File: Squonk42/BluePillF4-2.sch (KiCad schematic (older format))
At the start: 0 parts

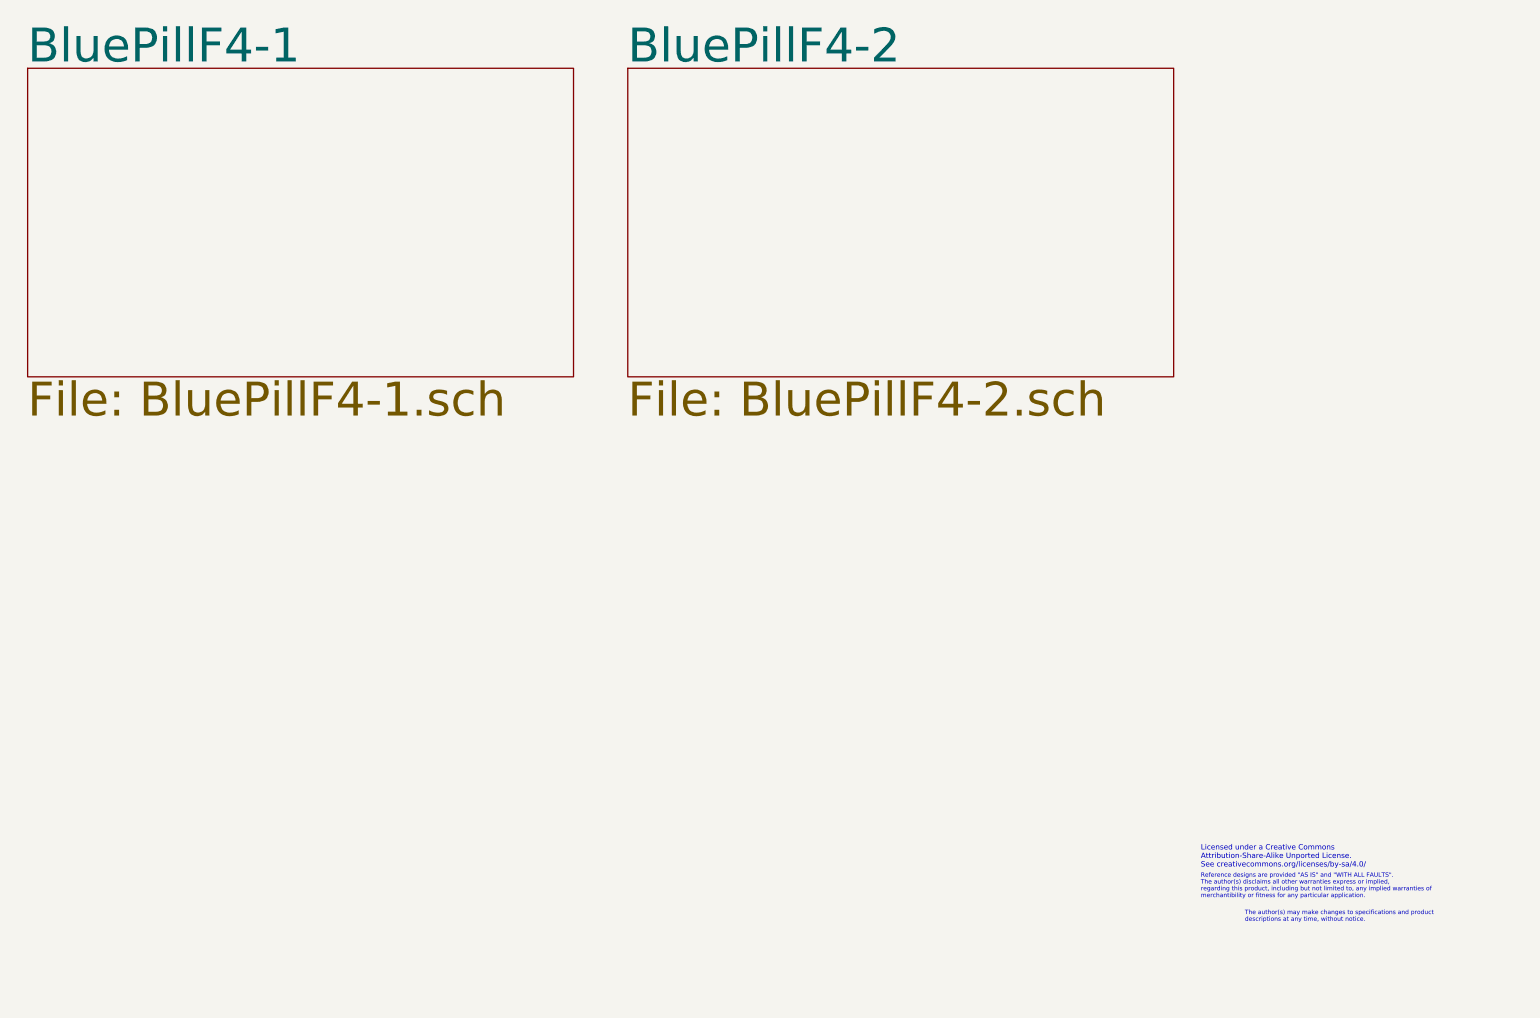
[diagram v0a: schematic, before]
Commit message: Added LiPo battery charger circuit (option) Put AGND on the analog LDO instead of GND Improved the analog power supply filter Aligned the pads for the PC1-PC7 pins with a 1.27 mm pitch. Now PC0 is used for VBUS_EN instead of PC4 previously
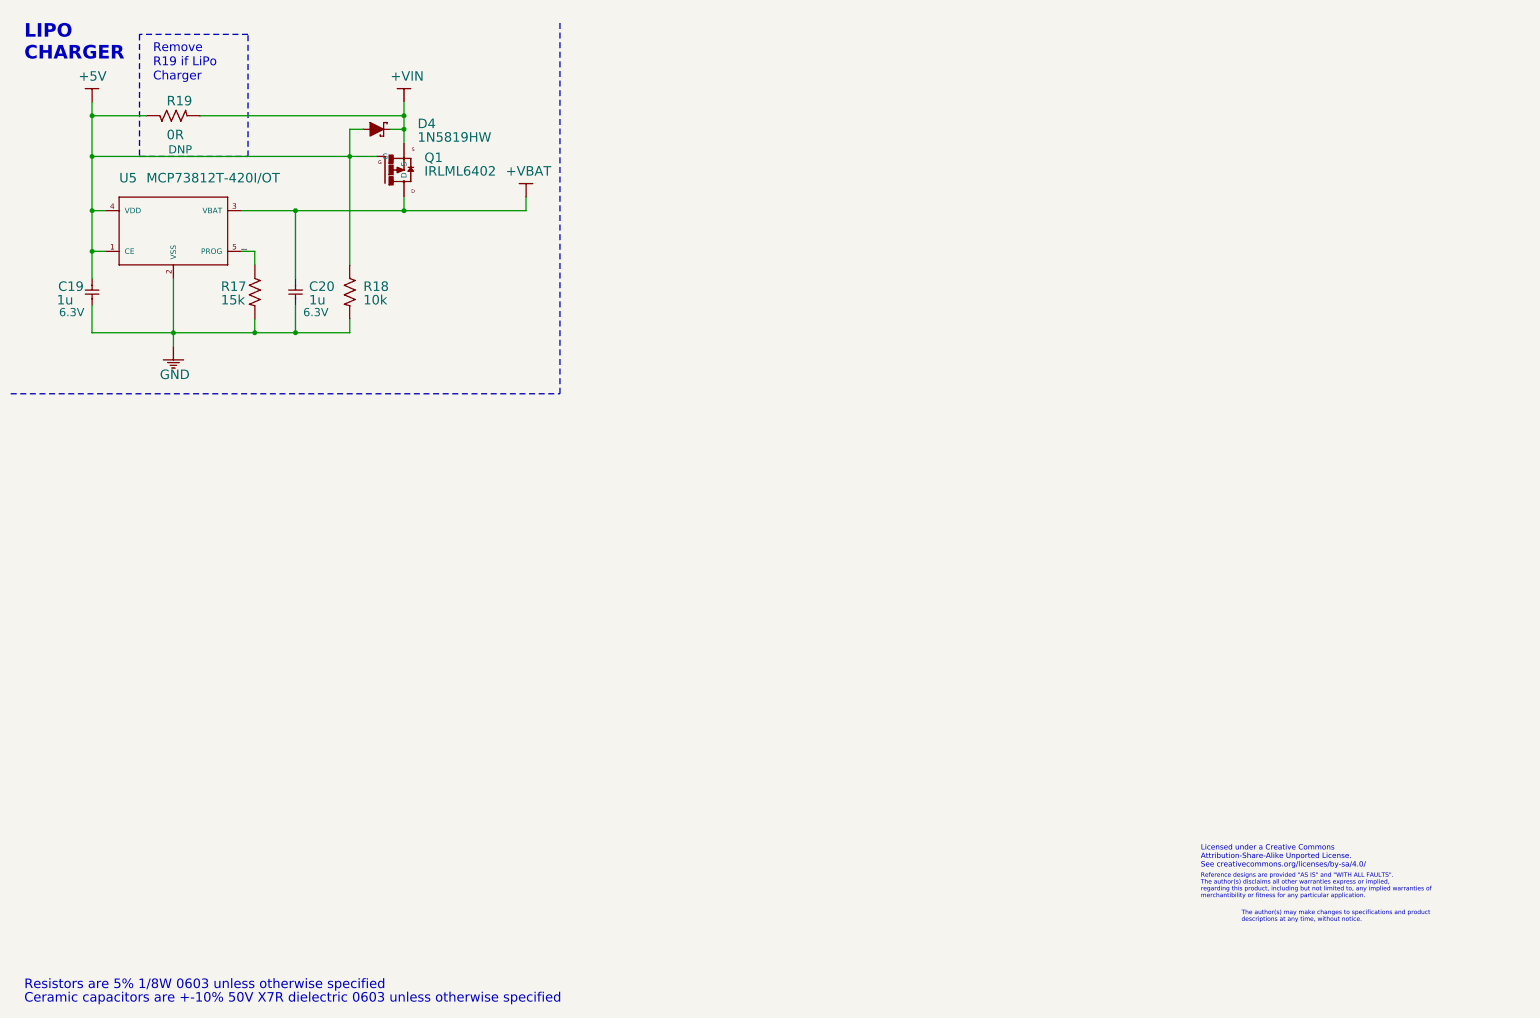
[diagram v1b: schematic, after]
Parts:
- added C19, C20: 1u, BluePillF4 Lib:C0603, symbol CAP_0603
- added D4: 1N5819HW, BluePillF4 Lib:SOD-123, symbol 1N5819HW
- added Q1: IRLML6402, BluePillF4 Lib:SOT323, symbol IRLML6402
- added R17: 15k, BluePillF4 Lib:R0603, symbol RES_0603
- added R18: 10k, BluePillF4 Lib:R0603, symbol RES_0603
- added R19: 0R, BluePillF4 Lib:R0603, symbol RES_0603
- added U5: MCP73812T-420I/OT, BluePillF4 Lib:SOT23-5, symbol MCP73812T-420I/OT
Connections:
- new net +5V: C19.1, D4.A, Q1.1 (G), R18.1, R19.1, U5.1 (CE), U5.4 (VDD)
- new net +VBAT: C20.1, Q1.3 (D), U5.3 (VBAT)
- new net +VIN: D4.C, Q1.2 (S), R19.2
- new net GND: C19.2, C20.2, R17.2, R18.2, U5.2 (VSS)
- new net PROG: R17.1, U5.5 (PROG)
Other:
- note added: "Ceramic capacitors are +-10% 50V X7R dielectric 0603 unless otherwise specified"
- note added: "LIPO\nCHARGER"
- note added: "Remove\nR19 if LiPo\nCharger"
- note added: "Resistors are 5% 1/8W 0603 unless otherwise specified"

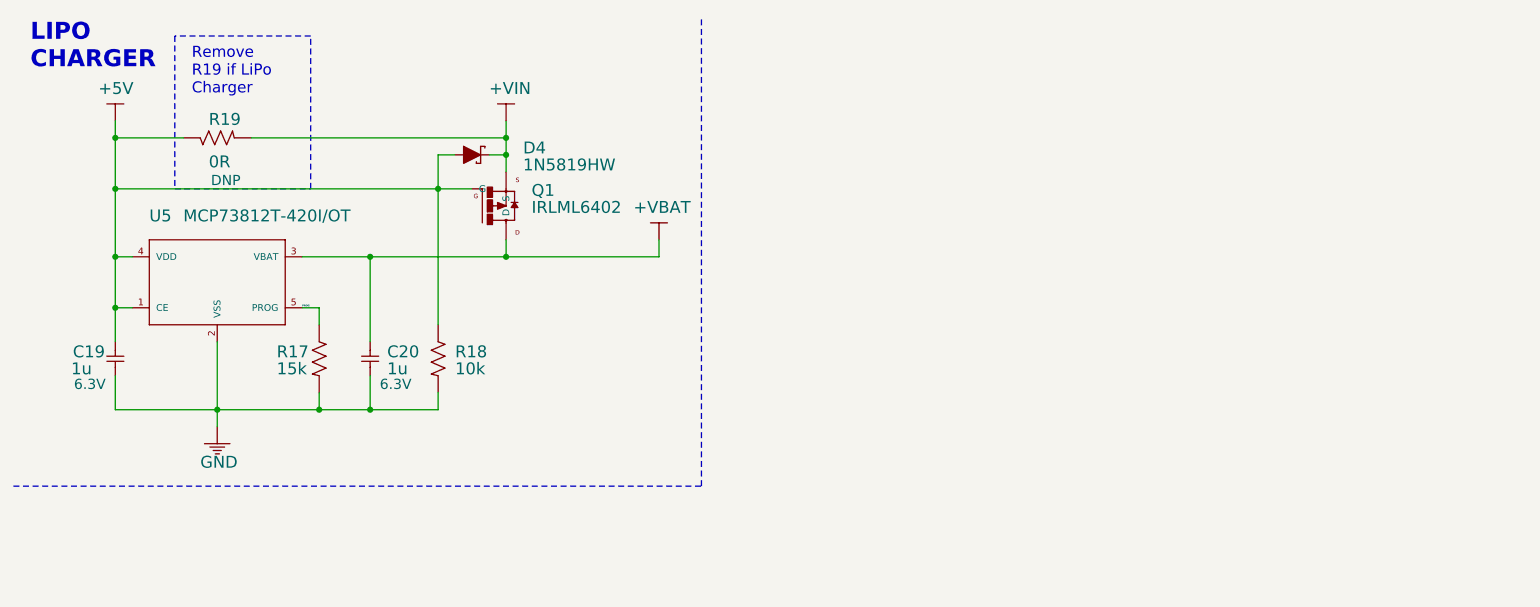
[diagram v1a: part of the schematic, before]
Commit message: Replaced the MicroSD Card connector with a Molex 47309-2651 Added voltage sense resistor divider Cleaned up traces
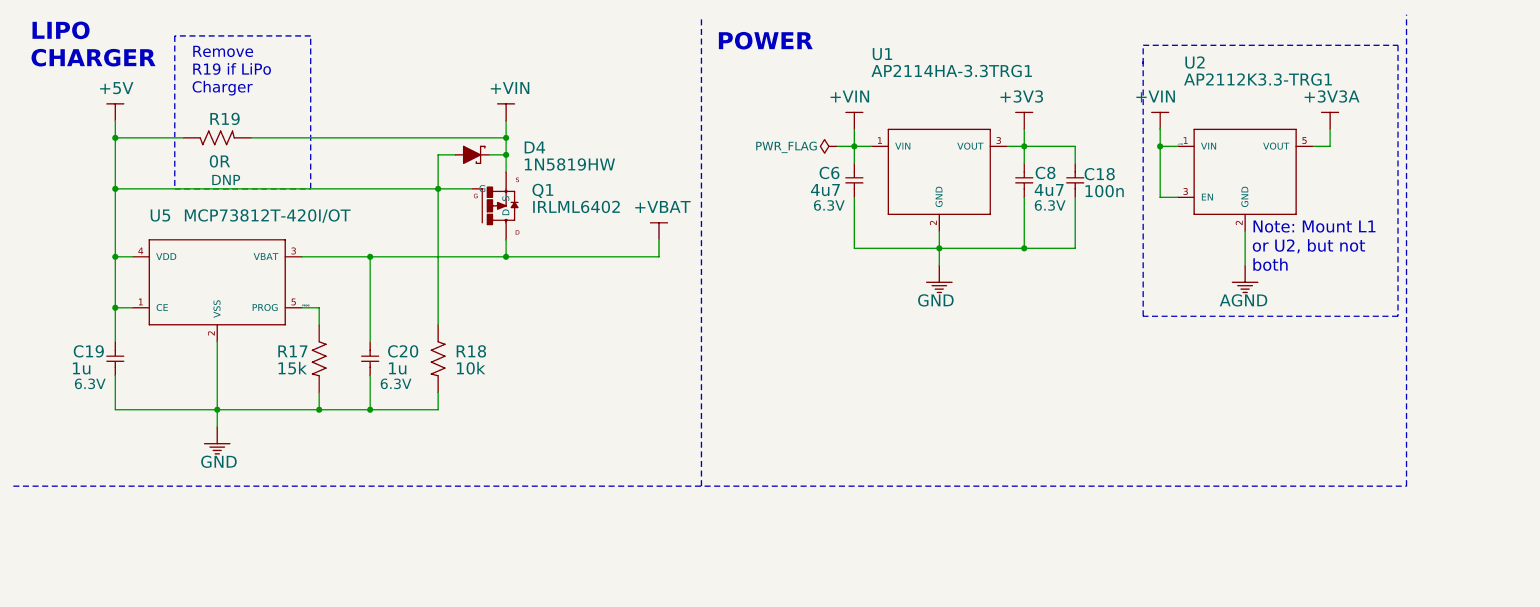
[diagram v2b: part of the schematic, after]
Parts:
- added C18: 100n, BluePillF4 Lib:C0603, symbol CAP_0603
- added C6, C8: 4u7, BluePillF4 Lib:C0603, symbol CAP_0603
- added U1: AP2114HA-3.3TRG1, BluePillF4 Lib:SOT223, symbol AP2114HA-3.3TRG1
- added U2: AP2112K3.3-TRG1, BluePillF4 Lib:SOT23-5, symbol AP2112K3.3-TRG1
- C19, C20: AliExpress (none) -> https://www.aliexpress.com/item/0603-SMD-Capacitor-assorted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
- D4: AliExpress (none) -> https://www.aliexpress.com/item/Livraison-gratuite-100-pcs-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
- Q1: AliExpress (none) -> https://www.aliexpress.com/item/Livraison-gratuite-20-PCS-I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
- R17: AliExpress (none) -> https://ww.aliexpress.com/store/product/300-pcs-lot-SMD-Puc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
- R18: AliExpress (none) -> https://www.aliexpress.com/item/Free-shipping-0603-SMD-Resi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
- R19: AliExpress (none) -> https://www.aliexpress.com/item/300-pcs-lot-SMD-Puce-R-sist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
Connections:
- net +VIN: now also C6.1, U1.1 (VIN), U2.1 (VIN), U2.3 (EN)
- net GND: now also C18.1, C6.2, C8.2, U1.2 (GND), U1.PAD (GND)
- new net +3V3: C18.2, C8.1, U1.3 (VOUT)
- new net +3V3A: U2.5 (VOUT)
- new net AGND: U2.2 (GND)
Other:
- note added: "Note: Mount L1\nor U2, but not\nboth"
- note added: "POWER"
